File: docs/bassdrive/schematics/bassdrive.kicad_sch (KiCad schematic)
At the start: 0 parts

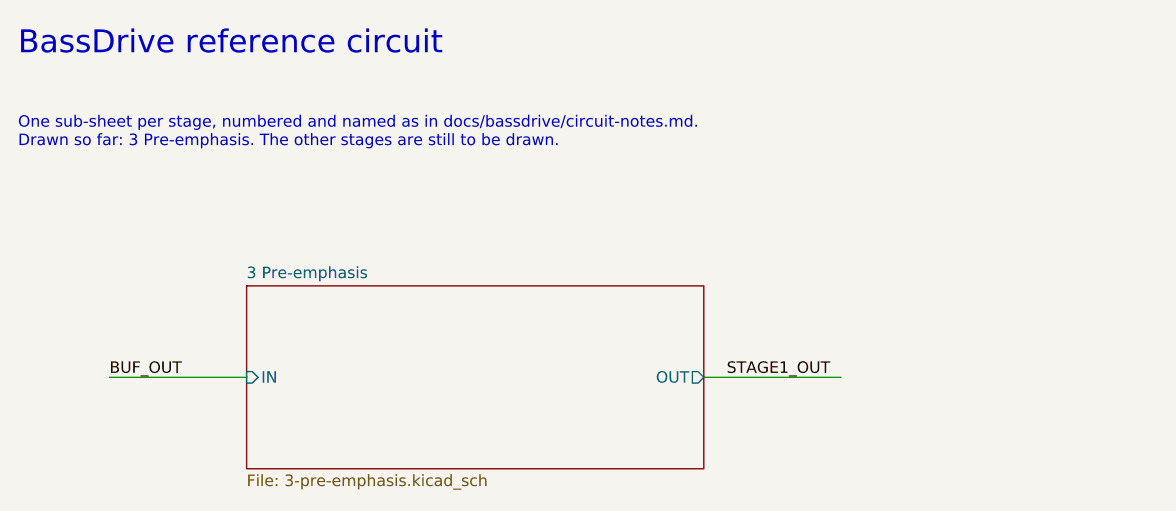
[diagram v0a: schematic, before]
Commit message: Mark the open sheet pins no-connect instead of labelling them
ERC reported the root sheet's BUF_OUT and STAGE1_OUT labels as dangling,
since nothing else on those nets is drawn yet.

Co-Authored-By: Claude Opus 5.5 <noreply@anthropic.com>
Claude-Session: https://claude.ai/code/session_01Mtxhexec2xasG4cja5raeU
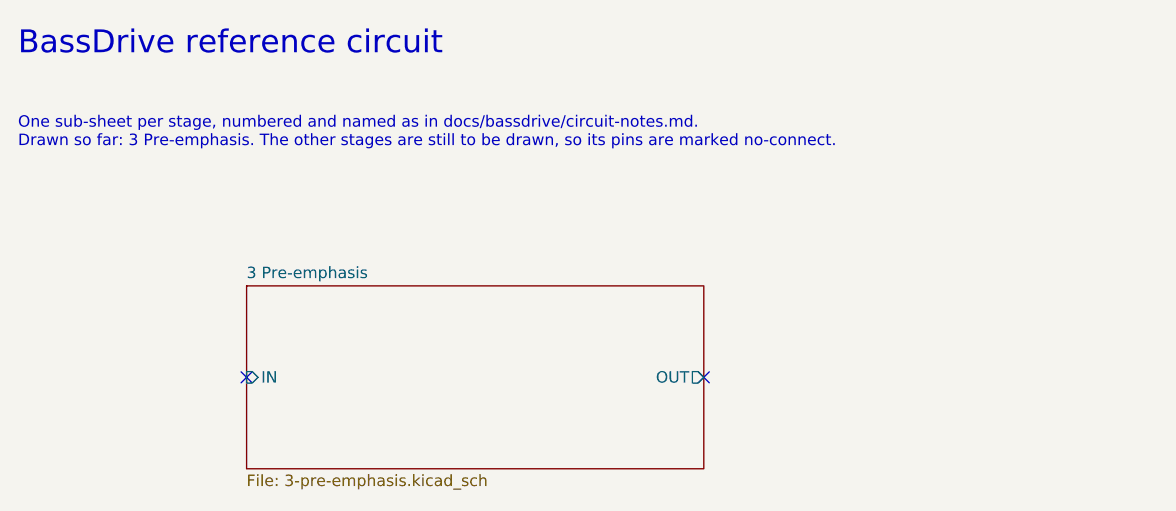
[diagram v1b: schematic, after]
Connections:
- no-connect marks 0 -> 2
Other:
- note added: "One sub-sheet per stage, numbered and named as in docs/bassdrive/circuit-notes.md. Drawn so far: 3 Pre-emphasis. The other stages are still to be drawn, so its pins are marked no-connect."
- note removed: "One sub-sheet per stage, numbered and named as in docs/bassdrive/circuit-notes.md. Drawn so far: 3 Pre-emphasis. The other stages are still to be drawn."
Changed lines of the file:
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@@
   )
   (sheet (at 101.6 71.12) (size 50.8 20.32) (fields_autoplaced yes) (stroke (width 0.1524) (type solid)) (fill (color 0 0 0 0.0000)) (property "Sheetname" "3 Pre-emphasis" (at 101.6 70.41 0) (effects (font (size 1.27 1.27)) (justify left bottom))) (property "Sheetfile" "3-pre-emphasis.kicad_sch" (at 101.6 92.03 0) (effects (font (size 1.27 1.27)) (justify left top))) (pin "IN" input (at 101.6 81.28 180) (effects (font (size 1.27 1.27)) (justify left))) (pin "OUT" output (at 152.4 81.28 0) (effects (font (size 1.27 1.27)) (justify right))) (instances (project "bassdrive" (path "/8ff94a34-916f-51d8-b34f-9197a04f87a8" (page "2")))))
-  (wire (pts (xy 86.36 81.28) (xy 101.6 81.28)) (stroke (width 0) (type default)))
-  (label "BUF_OUT" (at 86.36 81.28 0) (effects (font (size 1.27 1.27)) (justify left bottom)))
-  (wire (pts (xy 152.4 81.28) (xy 167.64 81.28)) (stroke (width 0) (type default)))
-  (label "STAGE1_OUT" (at 154.94 81.28 0) (effects (font (size 1.27 1.27)) (justify left bottom)))
+  (no_connect (at 101.6 81.28))
+  (no_connect (at 152.4 81.28))
   (text "BassDrive reference circuit" (exclude_from_sim no) (at 76.2 45.72 0) (effects (font (size 2.54 2.54)) (justify left bottom)))
-  (text "One sub-sheet per stage, numbered and named as in docs/bassdrive/circuit-notes.md.\nDrawn so far: 3 Pre-emphasis. The other stages are still to be drawn." (exclude_from_sim no) (at 76.2 55.88 0) (effects (font (size 1.27 1.27)) (justify left bottom)))
+  (text "One sub-sheet per stage, numbered and named as in docs/bassdrive/circuit-notes.md.\nDrawn so far: 3 Pre-emphasis. The other stages are still to be drawn, so its pins are marked no-connect." (exclude_from_sim no) (at 76.2 55.88 0) (effects (font (size 1.27 1.27)) (justify left bottom)))
   (sheet_instances (path "/" (page "1")))
 )

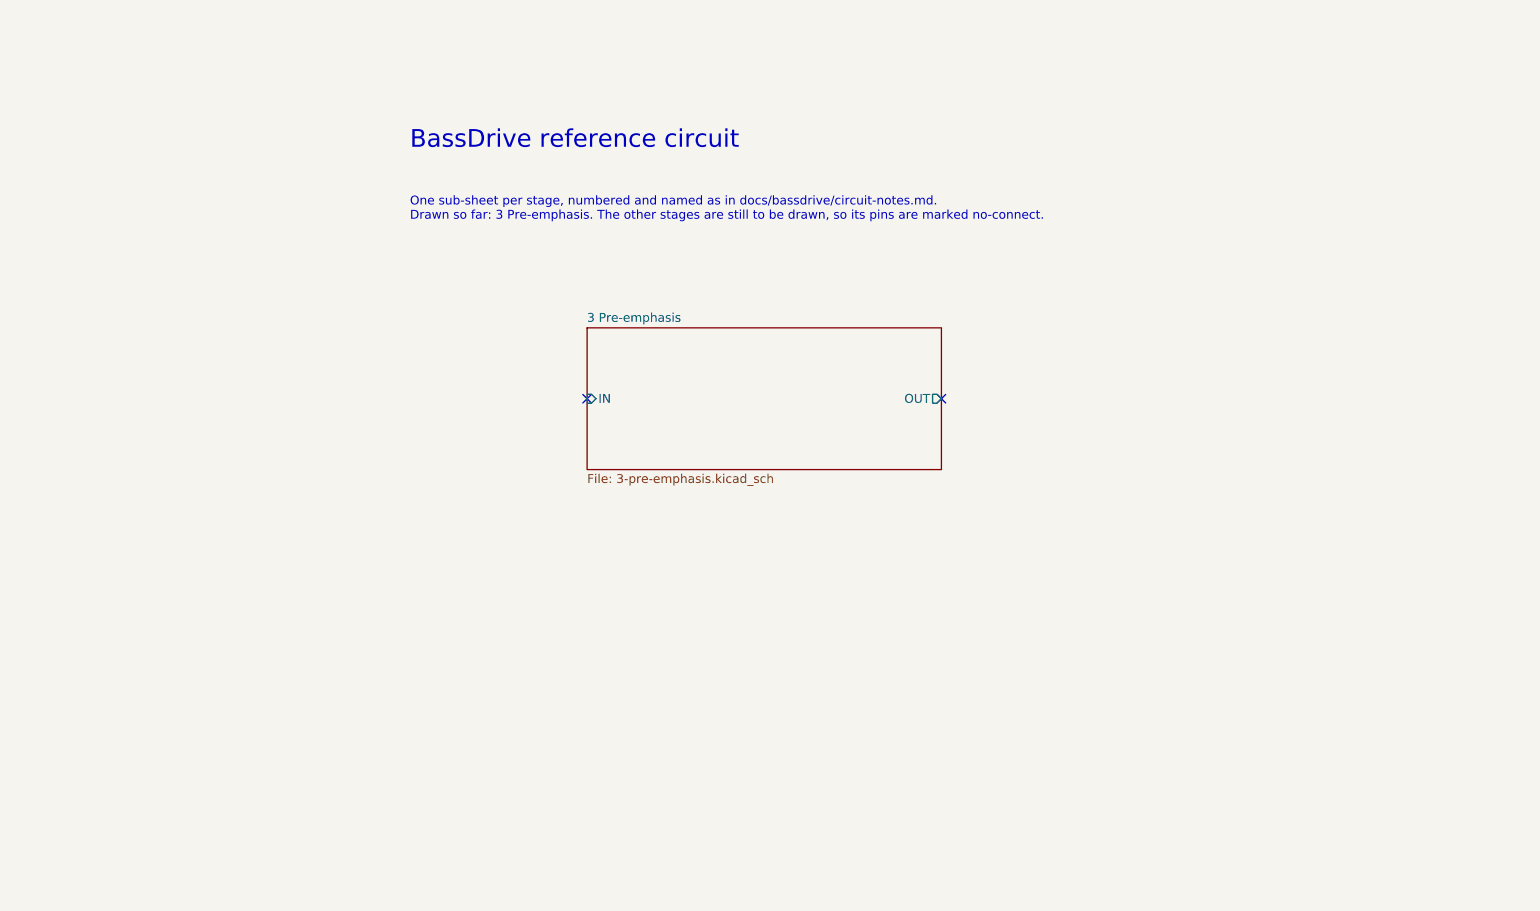
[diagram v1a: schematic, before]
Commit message: Generate KiCad schematics for every effect and make them standard (#85)
* chore: save work

* Generate KiCad schematics for every effect and make them standard (closes #11)

Every effect with circuit notes now has a KiCad schematic of its modelled
circuit, generated from tools/schematics/<name>.py by the new kicadsch and
stages modules: BassDrive (#11), BassPreamp and MidHump. Each script checks
its corner frequencies and gains against the notes and DSP constants.

make schematic-sources regenerates the sheets, make schematic-check (a new
docs-workflow step) fails if they are stale, and the schematics-present
pre-commit hook fails if an effect with circuit notes has none. AGENTS.md,
the effect skill and the developer guides now treat the schematic as a
required step. The sheets are embedded next to their sections in each
effect's circuit notes, and the disagreements drawing them revealed are
recorded as open questions.

Co-Authored-By: Claude Opus 5.5 <noreply@anthropic.com>

---------

Co-authored-by: Claude Opus 5.5 <noreply@anthropic.com>
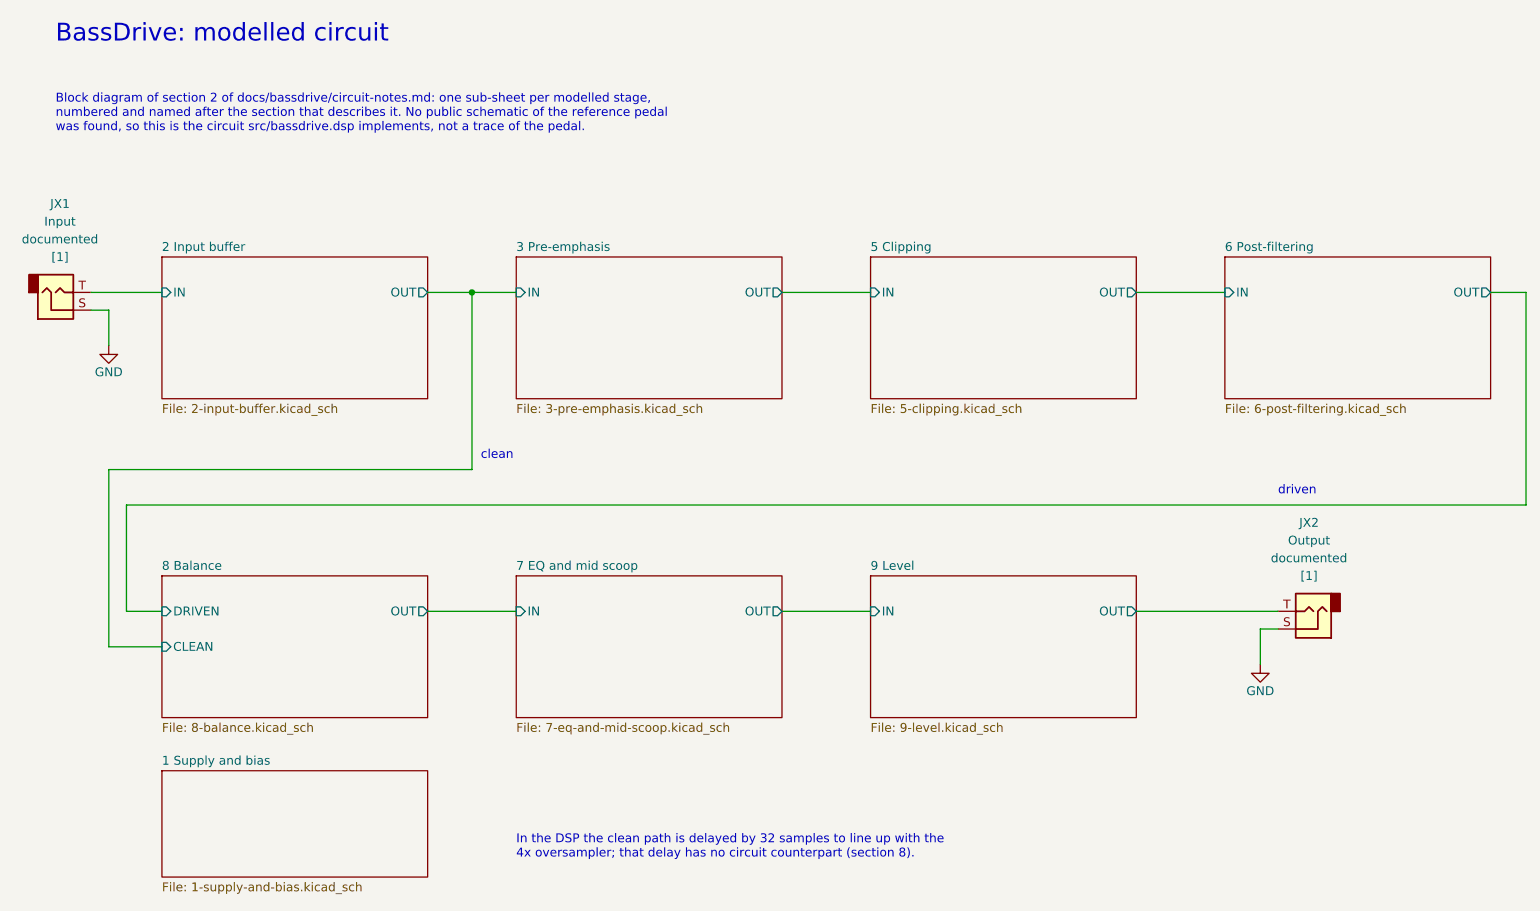
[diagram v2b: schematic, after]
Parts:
- added JX1: Input, symbol Connector_Audio:AudioJack2
- added JX2: Output, symbol Connector_Audio:AudioJack2
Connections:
- new net 2 Input buffer/IN: JX1.T
- new net 9 Level/OUT: JX2.T
- new net GND: JX1.S, JX2.S
- no-connect marks 2 -> 0
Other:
- added sheet 1 Supply and bias (1-supply-and-bias.kicad_sch)
- added sheet 2 Input buffer (2-input-buffer.kicad_sch)
- added sheet 5 Clipping (5-clipping.kicad_sch)
- added sheet 6 Post-filtering (6-post-filtering.kicad_sch)
- added sheet 7 EQ and mid scoop (7-eq-and-mid-scoop.kicad_sch)
- added sheet 8 Balance (8-balance.kicad_sch)
- added sheet 9 Level (9-level.kicad_sch)
- note added: "BassDrive: modelled circuit"
- note added: "Block diagram of section 2 of docs/bassdrive/circuit-notes.md: one sub-sheet per modelled stage, numbered and named after the section that describes it. No public schematic of the reference pedal was found, so this is the circuit src/bassdrive.dsp implements, not a trace of the pedal."
- note added: "In the DSP the clean path is delayed by 32 samples to line up with the 4x oversampler; that delay has no circuit counterpart (section 8)."
- note added: "clean"
- note added: "driven"
- note removed: "BassDrive reference circuit"
- note removed: "One sub-sheet per stage, numbered and named as in docs/bassdrive/circuit-notes.md. Drawn so far: 3 Pre-emphasis. The other stages are still to be drawn, so its pins are marked no-connect."
